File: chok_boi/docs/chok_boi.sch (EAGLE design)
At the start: 92 parts, among them U1 MPU-6000, U2 DRV8835

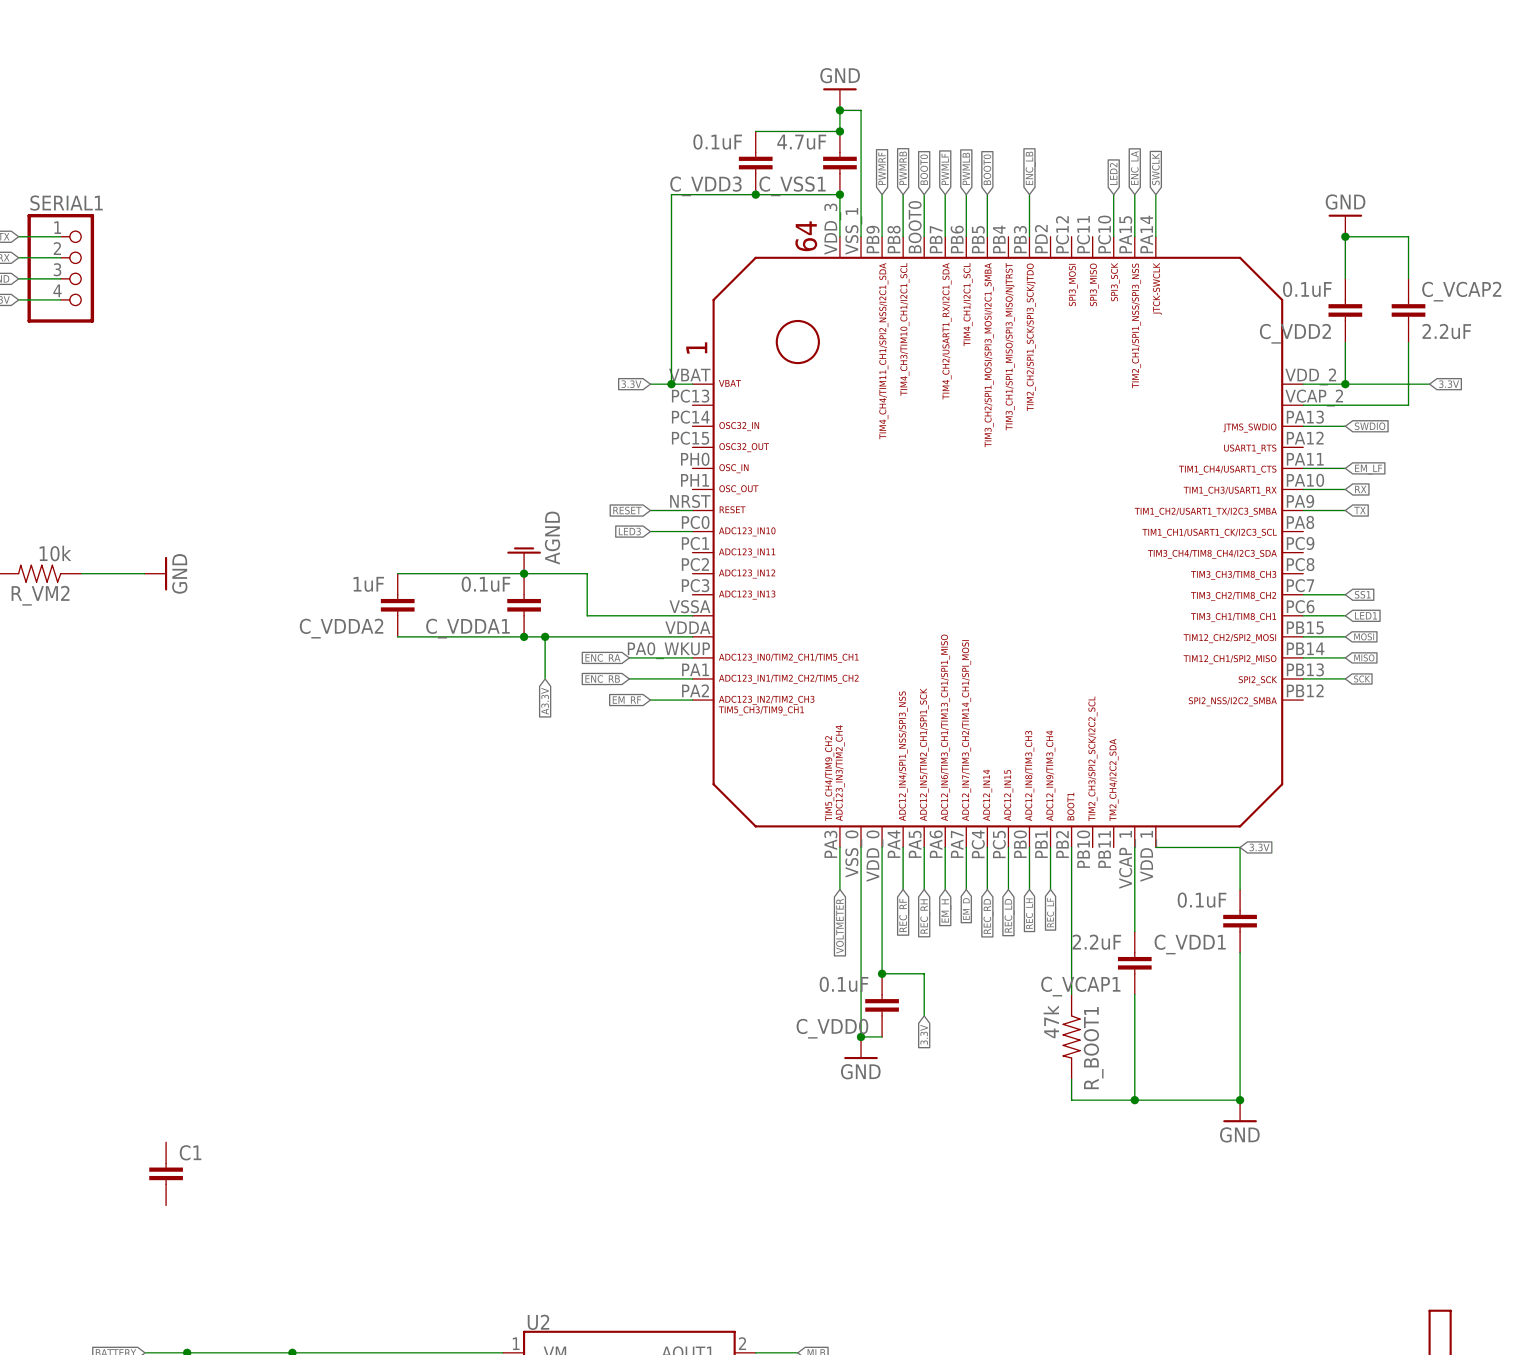
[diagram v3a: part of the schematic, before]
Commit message: Move LEDs on MCU and route more. 22 airwires left
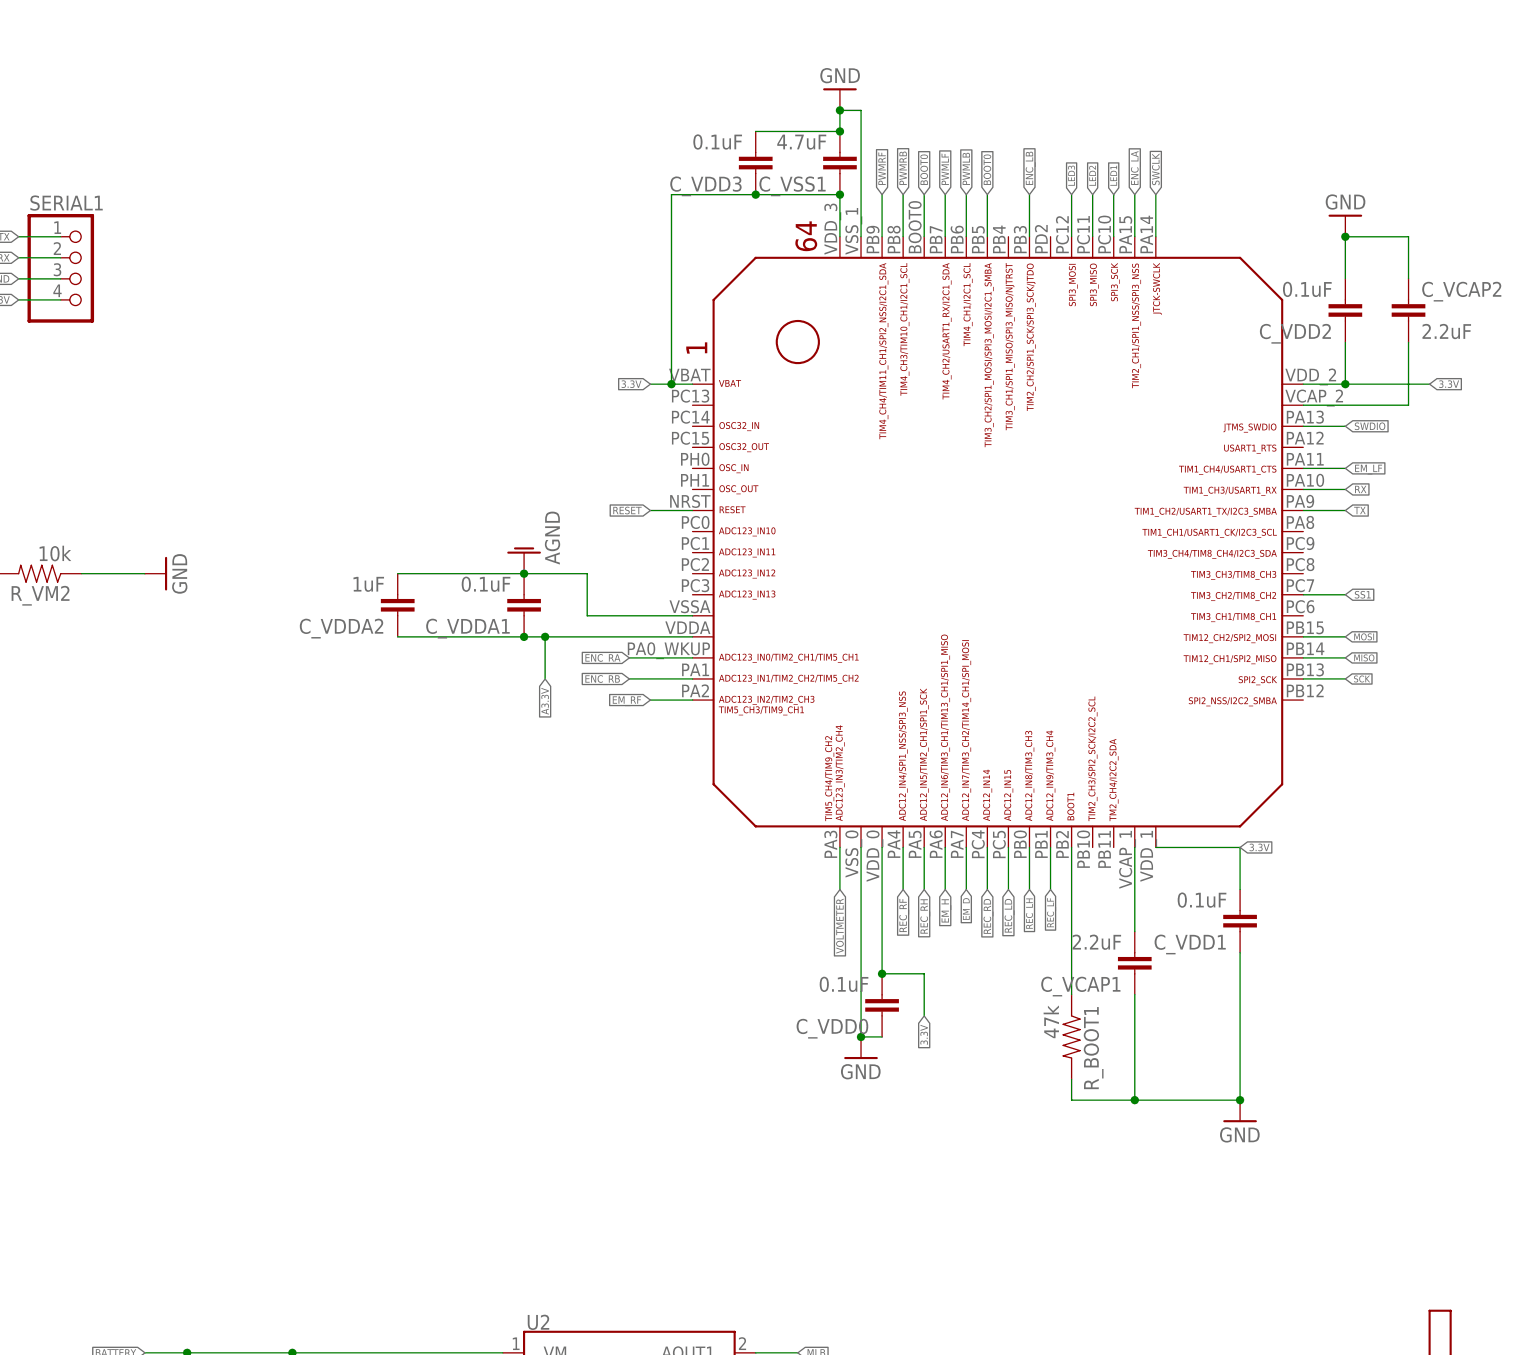
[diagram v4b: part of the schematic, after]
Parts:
- removed C1: (no value), SparkFun:CAP1210
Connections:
- net LED1: now also U$5.PC10; no longer U$5.PC6
- net LED2: now also U$5.PC11; no longer U$5.PC10
- net LED3: now also U$5.PC12; no longer U$5.PC0
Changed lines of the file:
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@@
 <?xml version="1.0" encoding="utf-8"?>
 <!DOCTYPE eagle SYSTEM "eagle.dtd">
-<eagle version="8.3.2">
+<eagle version="8.4.1">
 <drawing>
 <settings>
@@
 <part name="C_M2" library="SparkFun" deviceset="CAP" device="0603-CAP" value="0.1uF"/>
 <part name="C_MB" library="Volks73-Kemet" deviceset="T491?*" device="X" technology="107K025AT" value="100uF"/>
-<part name="C1" library="SparkFun" deviceset="CAP" device="1210"/>
 </parts>
 <sheets>
@@
 <instance part="C_M2" gate="G$1" x="-177.8" y="-177.8" rot="R180"/>
 <instance part="C_MB" gate="G$1" x="-190.5" y="-180.34"/>
-<instance part="C1" gate="G$1" x="-193.04" y="-149.86"/>
 </instances>
 <busses>
@@
 </segment>
 <segment>
-<pinref part="U$5" gate="G$1" pin="PC6"/>
-<wire x1="-55.88" y1="-81.28" x2="-50.8" y2="-81.28" width="0.1524" layer="91"/>
-<label x="-50.8" y="-81.28" size="0.889" layer="95" xref="yes"/>
+<pinref part="U$5" gate="G$1" pin="PC10"/>
+<wire x1="-78.74" y1="-35.56" x2="-78.74" y2="-30.48" width="0.1524" layer="91"/>
+<label x="-78.74" y="-30.48" size="0.8128" layer="95" rot="R90" xref="yes"/>
 </segment>
 </net>
@@
 </segment>
 <segment>
-<pinref part="U$5" gate="G$1" pin="PC10"/>
-<wire x1="-78.74" y1="-35.56" x2="-78.74" y2="-30.48" width="0.1524" layer="91"/>
-<label x="-78.74" y="-30.48" size="0.889" layer="95" rot="R90" xref="yes"/>
+<pinref part="U$5" gate="G$1" pin="PC11"/>
+<wire x1="-81.28" y1="-35.56" x2="-81.28" y2="-30.48" width="0.1524" layer="91"/>
+<label x="-81.28" y="-30.48" size="0.8128" layer="95" rot="R90" xref="yes"/>
 </segment>
 </net>
@@
 </segment>
 <segment>
-<pinref part="U$5" gate="G$1" pin="PC0"/>
-<wire x1="-129.54" y1="-71.12" x2="-134.62" y2="-71.12" width="0.1524" layer="91"/>
-<label x="-134.62" y="-71.12" size="0.889" layer="95" rot="R180" xref="yes"/>
-</segment>
-</net>
+<pinref part="U$5" gate="G$1" pin="PC12"/>
+<wire x1="-83.82" y1="-35.56" x2="-83.82" y2="-30.48" width="0.1524" layer="91"/>
+<label x="-83.82" y="-30.48" size="0.8128" layer="95" rot="R90" xref="yes"/>
+</segment>
+</net>

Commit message: Finish routing
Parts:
- removed R_BOOT1: 47k, SparkFun-Passives:RESISTOR0402-RES
- removed T1, T2, T3, T4: (no value), zetex:NPNSOT323
- added NMOS1, NMOS2, NMOS3, NMOS4: DMN3150LW, DMN3150LW:DMN3150LW
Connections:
- removed net N$10: R_BOOT1.1, U$5.PB2
- removed net N$23: R_ERF.1, T3.C
- new net N$5: NMOS3.D, R_ERF.1
- net EM_D: now also NMOS2.G; no longer T2.B
- net EM_H: now also NMOS4.G; no longer T4.B
- net EM_LF: now also NMOS1.G; no longer T1.B
- net EM_RF: now also NMOS3.G; no longer T3.B
- net GND: now also NMOS1.S, NMOS2.S, NMOS3.S, NMOS4.S, U$5.PB2; no longer R_BOOT1.2, T1.E, T2.E, T3.E, T4.E
- net INT: now also U$5.PB10
- net MLB: now also U2.BOUT1; no longer U2.AOUT1
- net MLF: now also U2.BOUT2; no longer U2.AOUT2
- net MODE: now also U$5.PB4
- net MRB: now also U2.AOUT1; no longer U2.BOUT1
- net MRF: now also U2.AOUT2; no longer U2.BOUT2
- net N$18: now also NMOS2.D; no longer T2.C
- net N$19: now also NMOS4.D; no longer T4.C
- net N$7: now also NMOS1.D; no longer T1.C
- net PWMLB: now also U$5.PB7, U2.BIN1/PH; no longer U$5.PB6, U2.AIN1/PH
- net PWMLF: now also U$5.PB6, U2.BIN2/EN; no longer U$5.PB7, U2.AIN2/EN
- net PWMRB: now also U$5.PB9, U2.AIN1/PH; no longer U$5.PB8, U2.BIN1/PH
- net PWMRF: now also U$5.PB8, U2.AIN2/EN; no longer U$5.PB9, U2.BIN2/EN

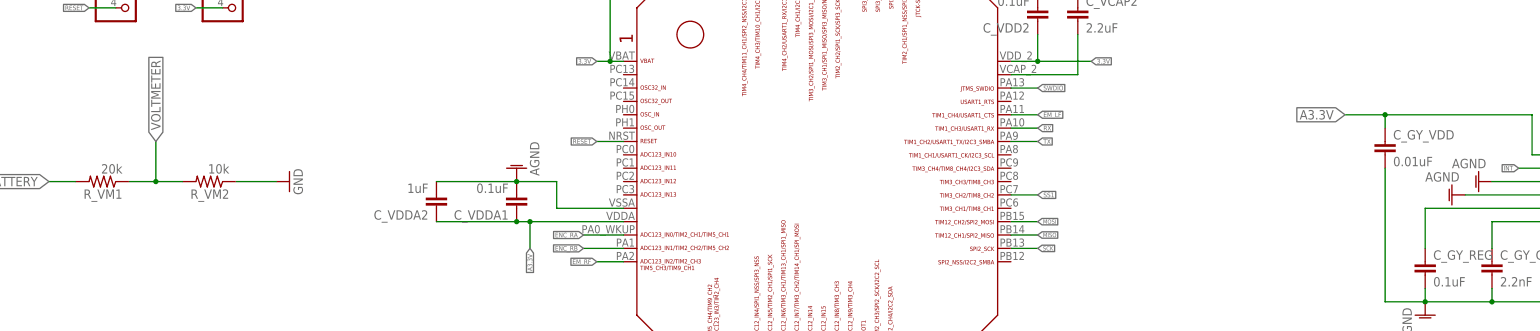
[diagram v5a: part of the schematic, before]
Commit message: Add text to PCB and change values of 2 passives
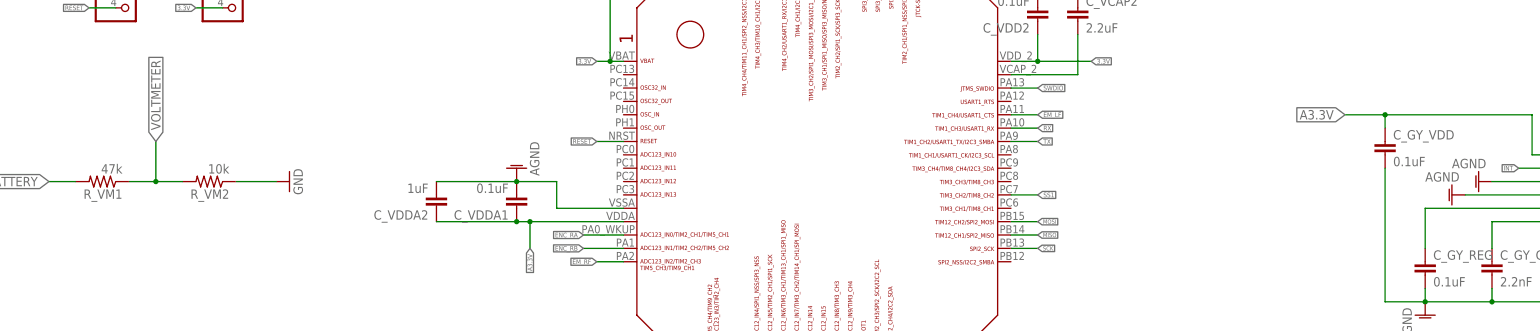
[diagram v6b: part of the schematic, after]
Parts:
- C_GY_VDD: value 0.01uF -> 0.1uF
- R_VM1: value 20k -> 47k
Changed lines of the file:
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@@
 <part name="C_ERF1" library="SparkFun-Capacitors" deviceset="CAP" device="0603-CAP" value="4.7uF"/>
 <part name="C_ERF2" library="SparkFun-Capacitors" deviceset="CAP" device="0603-CAP" value="0.1uF"/>
-<part name="R_VM1" library="SparkFun-Passives" deviceset="RESISTOR" device="0603-RES" value="20k"/>
+<part name="R_VM1" library="SparkFun-Passives" deviceset="RESISTOR" device="0603-RES" value="47k"/>
 <part name="R_VM2" library="SparkFun-Passives" deviceset="RESISTOR" device="0603-RES" value="10k"/>
 <part name="GND13" library="SparkFun-Aesthetics" deviceset="GND" device=""/>
@@
 <part name="C_GY_REG" library="SparkFun" deviceset="CAP" device="0603-CAP" value="0.1uF"/>
 <part name="C_GY_CP" library="SparkFun" deviceset="CAP" device="0603-CAP" value="2.2nF"/>
-<part name="C_GY_VDD" library="SparkFun" deviceset="CAP" device="0603-CAP" value="0.01uF"/>
+<part name="C_GY_VDD" library="SparkFun" deviceset="CAP" device="0603-CAP" value="0.1uF"/>
 <part name="AGND5" library="supply1" library_urn="urn:adsk.eagle:library:371" deviceset="AGND" device=""/>
 <part name="AGND2" library="supply1" library_urn="urn:adsk.eagle:library:371" deviceset="AGND" device=""/>
